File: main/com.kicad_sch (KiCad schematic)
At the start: 4 parts, among them J8 Conn_ARM_JTAG_SWD_10

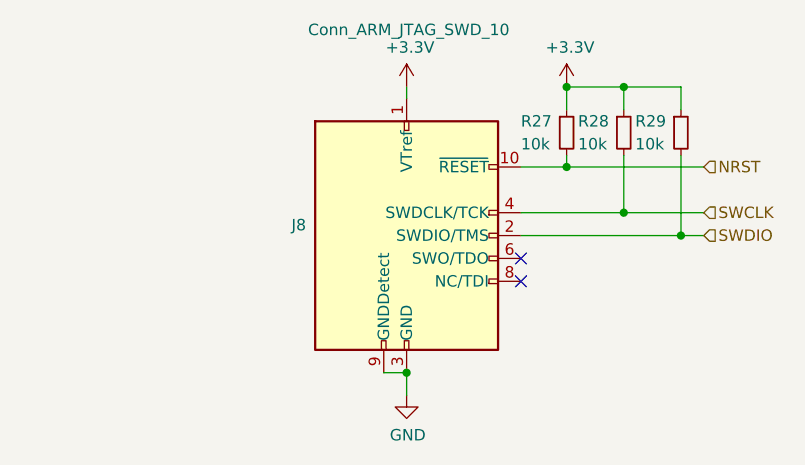
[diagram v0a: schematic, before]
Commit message: feat: update main board
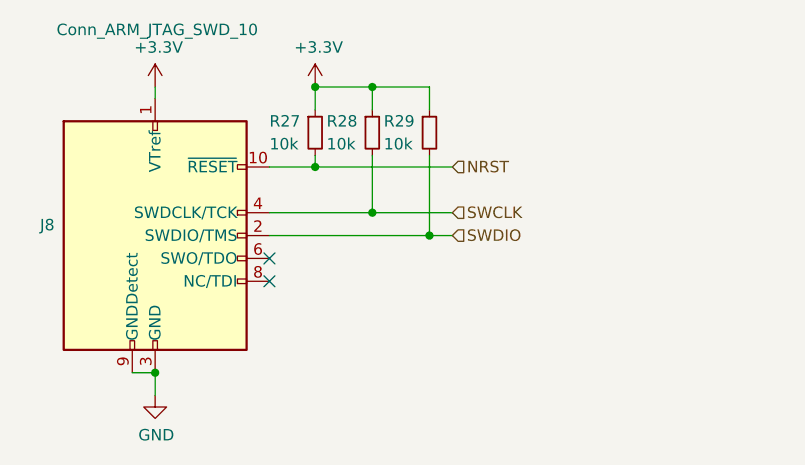
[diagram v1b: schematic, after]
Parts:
- J8: footprint Connector_PinHeader_1.27mm:PinHeader_2x05_P1.27mm_Vertical_SMD -> Connector_PinHeader_1.27mm:PinHeader_2x05_P1.27mm_Vertical
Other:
- moved on the sheet: J8, R27, R28, R29
